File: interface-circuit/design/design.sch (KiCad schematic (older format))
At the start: 30 parts, among them J1 Raspberry_Pi_2_3, J10 Conn_01x02_Male, J11 Conn_01x03_Male, J12 Conn_01x03_Male, J13 Screw_Terminal_01x02, J14 Conn_01x02_Male, J2 Screw_Terminal_01x05, J3 Screw_Terminal_01x05, J4 Conn_02x15_Counter_Clockwise, J5 Conn_02x06_Counter_Clockwise, J6 Conn_01x02_Male, J7 Screw_Terminal_01x02, J8 Screw_Terminal_01x02, J9 Conn_01x02_Male, Q1 2N3904-AP, Q2 2N3904-AP, Q3 2N3904-AP, SW1 SW_SPST, SW2 SW_SPST, U1 LogicLevelConverter_BOB-08745

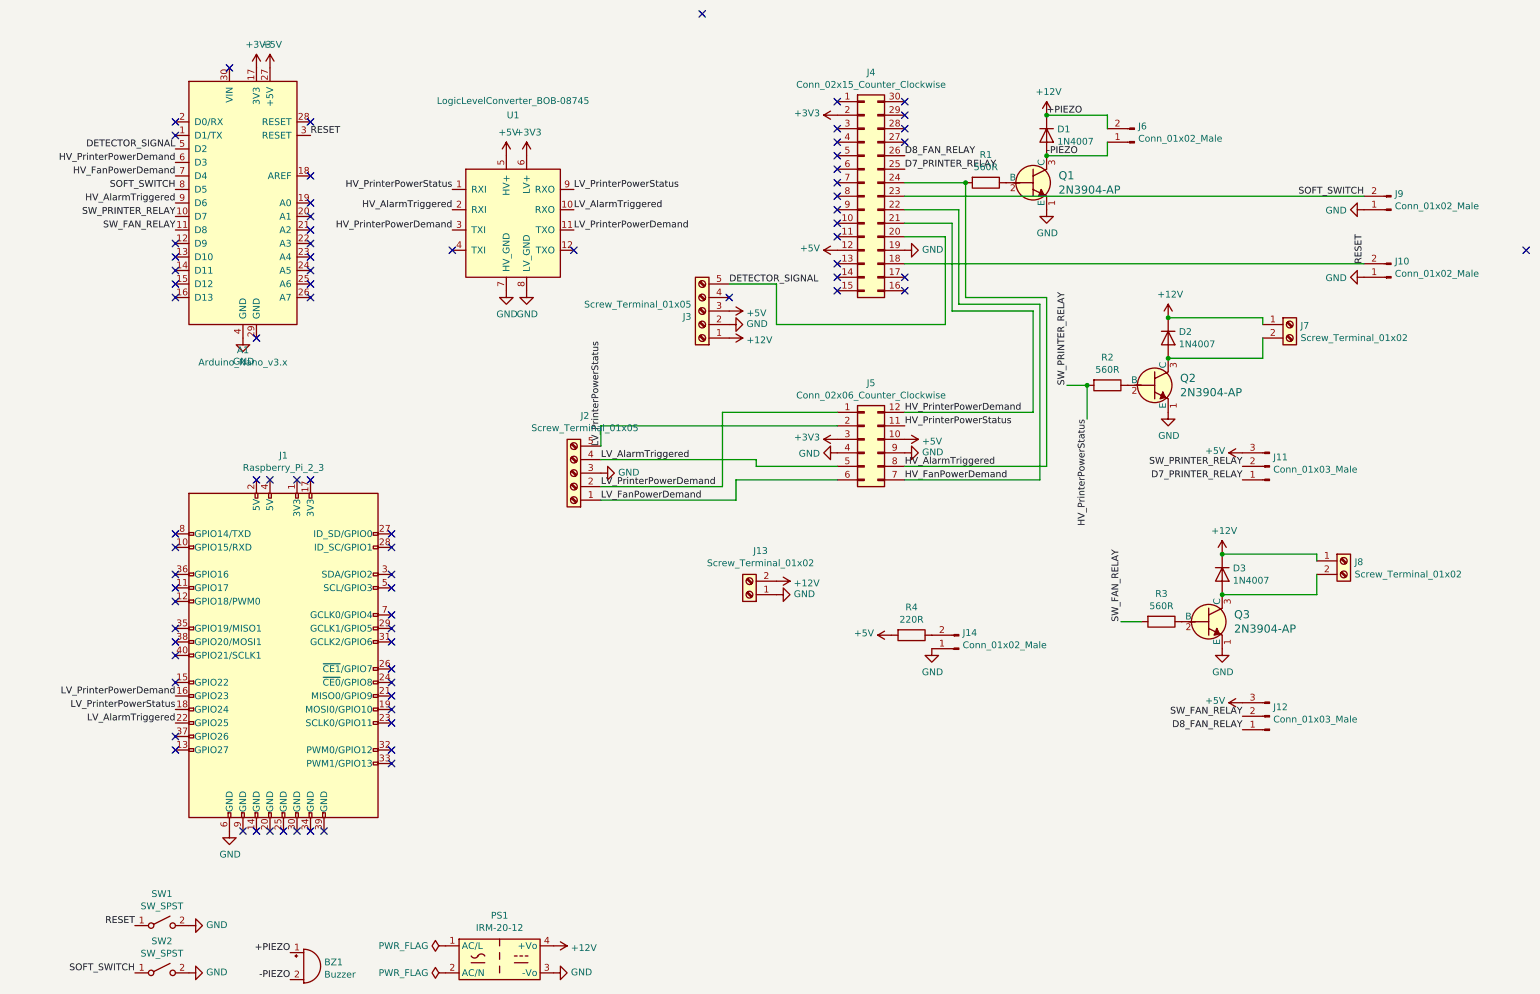
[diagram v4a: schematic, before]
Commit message: Removed connectors between Arduino and shifter, header strips will be soldered in under them
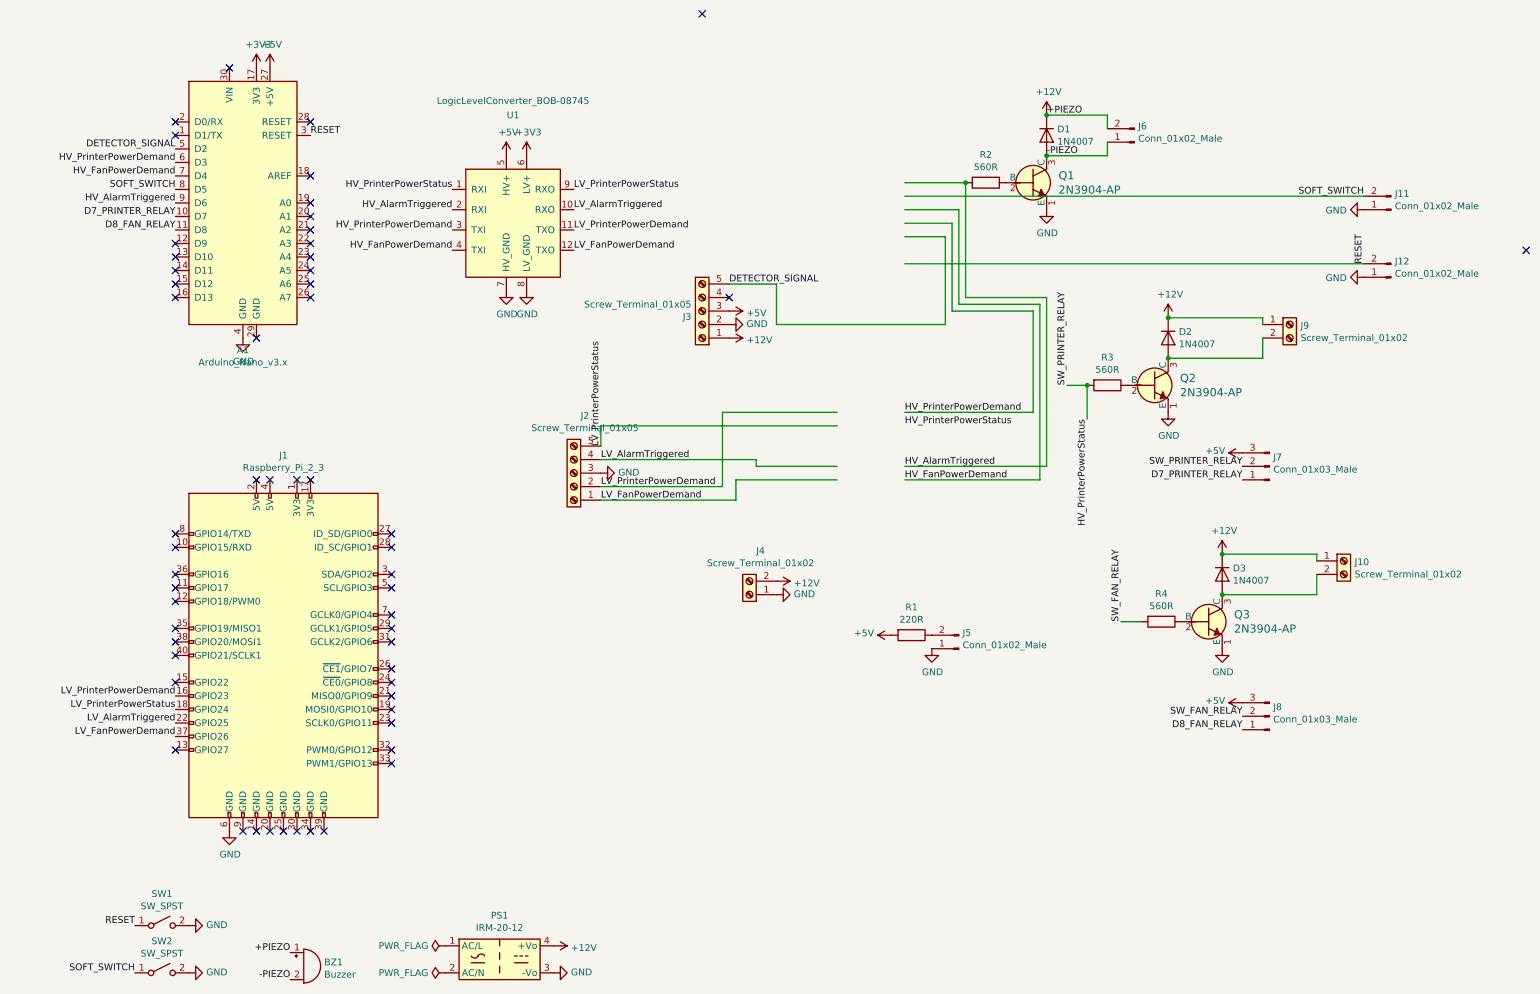
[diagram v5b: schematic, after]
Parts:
- removed J4: Conn_02x15_Counter_Clockwise, symbol Connector_Generic:Conn_02x15_Counter_Clockwise
- removed J5: Conn_02x06_Counter_Clockwise, symbol Connector_Generic:Conn_02x06_Counter_Clockwise
- renumbered J8 to J10, J9 to J11, J10 to J12, J13 to J4, J14 to J5, J11 to J7, J12 to J8, J7 to J9, R4 to R1, R1 to R2, R2 to R3, R3 to R4
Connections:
- no-connect marks 79 -> 57

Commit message: Cleanup
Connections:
- wire segments 48 -> 16
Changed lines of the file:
@@
 LV_AlarmTriggered
 Wire Wire Line
-	4650 3800 5550 3800
-Wire Wire Line
-	5550 3800 5550 3250
-Wire Wire Line
-	5550 3250 6400 3250
-Wire Wire Line
 	4650 3500 4650 3350
-Wire Wire Line
-	4650 3350 6400 3350
-Wire Wire Line
-	4650 3600 5800 3600
-Wire Wire Line
-	5800 3600 5800 3650
 $Comp
 L power:GND #PWR013
@@
 Text Label 4450 1900 0    50   ~ 0
 LV_PrinterPowerDemand
-Text Label 6900 3250 0    50   ~ 0
-HV_PrinterPowerDemand
-Text Label 6900 3350 0    50   ~ 0
-HV_PrinterPowerStatus
 $Comp
 L Connector:Conn_01x02_Male J12
@@
 NoConn ~ 5400 300
 NoConn ~ 5600 2400
-Wire Wire Line
-	5600 2300 5950 2300
-Wire Wire Line
-	5950 2300 5950 2600
-Wire Wire Line
-	5950 2600 7200 2600
-Wire Wire Line
-	7200 2600 7200 1950
-Wire Wire Line
-	7200 1950 6900 1950
-Wire Wire Line
-	6900 3250 7850 3250
-Wire Wire Line
-	7850 3250 7850 2500
-Wire Wire Line
-	7850 2500 7250 2500
-Wire Wire Line
-	7250 2500 7250 1850
-Wire Wire Line
-	7250 1850 6900 1850
 $Comp
 L Connector:Screw_Terminal_01x05 J2
@@
 	-1   0    0    1
 $EndComp
-Wire Wire Line
-	4650 3900 5650 3900
-Wire Wire Line
-	5650 3900 5650 3750
 Text Label 4650 3900 0    50   ~ 0
 LV_FanPowerDemand
-Wire Wire Line
-	7900 2450 7300 2450
-Wire Wire Line
-	7300 2450 7300 1750
-Wire Wire Line
-	7300 1750 6900 1750
-Wire Wire Line
-	6900 2150 10300 2150
 NoConn ~ 11500 2050
 $Comp
@@
 	0    1    1    0
 $EndComp
-Wire Wire Line
-	6900 1650 10300 1650
 Text Label 10300 1650 2    50   ~ 0
 SOFT_SWITCH
@@
 Text Label 1200 7400 2    50   ~ 0
 SOFT_SWITCH
-Wire Wire Line
-	7950 2400 7350 2400
-Wire Wire Line
-	7350 2400 7350 1550
-Wire Wire Line
-	7350 1550 6900 1550
 $Comp
 L Device:R R2
@@
 	0    1    1    0
 $EndComp
-Connection ~ 7350 1550
 $Comp
 L dk_Transistors-Bipolar-BJT-Single:2N3904-AP Q1
@@
 	0    -1   -1   0
 $EndComp
-Wire Wire Line
-	7950 3650 7950 2400
-Wire Wire Line
-	6900 3650 7950 3650
-Wire Wire Line
-	7900 3750 7900 2450
-Wire Wire Line
-	6900 3750 7900 3750
-Text Label 6900 3750 0    50   ~ 0
-HV_FanPowerDemand
-Wire Wire Line
-	5650 3750 6400 3750
-Text Label 6900 3650 0    50   ~ 0
-HV_AlarmTriggered
-Wire Wire Line
-	5800 3650 6400 3650
 Text Label 1500 5650 2    50   ~ 0
 LV_FanPowerDemand
@@
 Text Label 3550 2050 2    50   ~ 0
 HV_FanPowerDemand
+Text Label 7350 1550 2    50   ~ 0
+HV_AlarmTriggered
 $EndSCHEMATC

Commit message: Associated all components that will go on the protoboard
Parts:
- BZ1: footprint (none) -> Buzzer_Beeper:Buzzer_15x7.5RM7.6
- J10, J4, J9: footprint (none) -> Connectors:SCREWTERMINAL-5MM-2
- J11, J12, J5, J6: footprint (none) -> Connector_PinHeader_2.54mm:PinHeader_1x02_P2.54mm_Vertical
- J2, J3: footprint (none) -> Connectors:SCREWTERMINAL-3.5MM-5
- J7, J8: footprint (none) -> Connector_PinHeader_2.54mm:PinHeader_1x03_P2.54mm_Vertical
- R1, R2, R3, R4: footprint (none) -> Resistor_THT:R_Axial_DIN0207_L6.3mm_D2.5mm_P10.16mm_Horizontal
- U1: footprint (none) -> custom-footprints:LOGIC_LEVEL_CONVERTER_BOB11978_BOB8745_XC4486
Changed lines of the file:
@@
 F 0 "U1" H 4000 2650 50  0000 C CNN
 F 1 "LogicLevelConverter_BOB-08745" H 4000 2756 50  0000 C CNN
-F 2 "" H 3350 2600 50  0001 C CNN
+F 2 "custom-footprints:LOGIC_LEVEL_CONVERTER_BOB11978_BOB8745_XC4486" H 3350 2600 50  0001 C CNN
 F 3 "" H 3350 2600 50  0001 C CNN
 	1    4000 1850
@@
 F 0 "J12" H 10472 2132 50  0000 R CNN
 F 1 "Conn_01x02_Male" H 10472 2223 50  0000 R CNN
-F 2 "" H 10500 2250 50  0001 C CNN
+F 2 "Connector_PinHeader_2.54mm:PinHeader_1x02_P2.54mm_Vertical" H 10500 2250 50  0001 C CNN
 F 3 "~" H 10500 2250 50  0001 C CNN
 	1    10500 2250
@@
 F 0 "J3" H 5480 2542 50  0000 L CNN
 F 1 "Screw_Terminal_01x05" H 5480 2451 50  0000 L CNN
-F 2 "" H 5400 2500 50  0001 C CNN
+F 2 "Connectors:SCREWTERMINAL-3.5MM-5" H 5400 2500 50  0001 C CNN
 F 3 "~" H 5400 2500 50  0001 C CNN
 	1    5400 2500
@@
 F 0 "J2" H 4368 3275 50  0000 C CNN
 F 1 "Screw_Terminal_01x05" H 4368 3366 50  0000 C CNN
-F 2 "" H 4450 3700 50  0001 C CNN
+F 2 "Connectors:SCREWTERMINAL-3.5MM-5" H 4450 3700 50  0001 C CNN
 F 3 "~" H 4450 3700 50  0001 C CNN
 	1    4450 3700
@@
 F 0 "J11" H 10472 1632 50  0000 R CNN
 F 1 "Conn_01x02_Male" H 10472 1723 50  0000 R CNN
-F 2 "" H 10500 1750 50  0001 C CNN
+F 2 "Connector_PinHeader_2.54mm:PinHeader_1x02_P2.54mm_Vertical" H 10500 1750 50  0001 C CNN
 F 3 "~" H 10500 1750 50  0001 C CNN
 	1    10500 1750
@@
 F 0 "R2" V 7293 1550 50  0000 C CNN
 F 1 "560R" V 7384 1550 50  0000 C CNN
-F 2 "" V 7430 1550 50  0001 C CNN
+F 2 "Resistor_THT:R_Axial_DIN0207_L6.3mm_D2.5mm_P10.16mm_Horizontal" V 7430 1550 50  0001 C CNN
 F 3 "~" H 7500 1550 50  0001 C CNN
 	1    7500 1550
@@
 F 0 "J6" H 8572 1132 50  0000 R CNN
 F 1 "Conn_01x02_Male" H 8572 1223 50  0000 R CNN
-F 2 "" H 8600 1250 50  0001 C CNN
+F 2 "Connector_PinHeader_2.54mm:PinHeader_1x02_P2.54mm_Vertical" H 8600 1250 50  0001 C CNN
 F 3 "~" H 8600 1250 50  0001 C CNN
 	1    8600 1250
@@
 F 0 "BZ1" H 2602 7379 50  0000 L CNN
 F 1 "Buzzer" H 2602 7288 50  0000 L CNN
-F 2 "" V 2425 7450 50  0001 C CNN
+F 2 "Buzzer_Beeper:Buzzer_15x7.5RM7.6" V 2425 7450 50  0001 C CNN
 F 3 "~" V 2425 7450 50  0001 C CNN
 	1    2450 7350
@@
 F 0 "R3" V 8193 3050 50  0000 C CNN
 F 1 "560R" V 8284 3050 50  0000 C CNN
-F 2 "" V 8330 3050 50  0001 C CNN
+F 2 "Resistor_THT:R_Axial_DIN0207_L6.3mm_D2.5mm_P10.16mm_Horizontal" V 8330 3050 50  0001 C CNN
 F 3 "~" H 8400 3050 50  0001 C CNN
 	1    8400 3050
@@
 F 0 "J9" H 9830 2592 50  0000 L CNN
 F 1 "Screw_Terminal_01x02" H 9830 2501 50  0000 L CNN
-F 2 "" H 9750 2600 50  0001 C CNN
+F 2 "Connectors:SCREWTERMINAL-5MM-2" H 9750 2600 50  0001 C CNN
 F 3 "~" H 9750 2600 50  0001 C CNN
 	1    9750 2600
@@
 F 0 "R4" V 8593 4800 50  0000 C CNN
 F 1 "560R" V 8684 4800 50  0000 C CNN
-F 2 "" V 8730 4800 50  0001 C CNN
+F 2 "Resistor_THT:R_Axial_DIN0207_L6.3mm_D2.5mm_P10.16mm_Horizontal" V 8730 4800 50  0001 C CNN
 F 3 "~" H 8800 4800 50  0001 C CNN
 	1    8800 4800
@@
 F 0 "J10" H 10230 4342 50  0000 L CNN
 F 1 "Screw_Terminal_01x02" H 10230 4251 50  0000 L CNN
-F 2 "" H 10150 4350 50  0001 C CNN
+F 2 "Connectors:SCREWTERMINAL-5MM-2" H 10150 4350 50  0001 C CNN
 F 3 "~" H 10150 4350 50  0001 C CNN
 	1    10150 4350
@@
 F 0 "J7" H 9572 3582 50  0000 R CNN
 F 1 "Conn_01x03_Male" H 9572 3673 50  0000 R CNN
-F 2 "" H 9600 3650 50  0001 C CNN
+F 2 "Connector_PinHeader_2.54mm:PinHeader_1x03_P2.54mm_Vertical" H 9600 3650 50  0001 C CNN
 F 3 "~" H 9600 3650 50  0001 C CNN
 	1    9600 3650
@@
 F 0 "J8" H 9572 5432 50  0000 R CNN
 F 1 "Conn_01x03_Male" H 9572 5523 50  0000 R CNN
-F 2 "" H 9600 5500 50  0001 C CNN
+F 2 "Connector_PinHeader_2.54mm:PinHeader_1x03_P2.54mm_Vertical" H 9600 5500 50  0001 C CNN
 F 3 "~" H 9600 5500 50  0001 C CNN
 	1    9600 5500
@@
 F 0 "J4" H 5668 4275 50  0000 C CNN
 F 1 "Screw_Terminal_01x02" H 5668 4366 50  0000 C CNN
-F 2 "" H 5750 4600 50  0001 C CNN
+F 2 "Connectors:SCREWTERMINAL-5MM-2" H 5750 4600 50  0001 C CNN
 F 3 "~" H 5750 4600 50  0001 C CNN
 	1    5750 4600
@@
 F 0 "R1" V 6743 4900 50  0000 C CNN
 F 1 "220R" V 6834 4900 50  0000 C CNN
-F 2 "" V 6880 4900 50  0001 C CNN
+F 2 "Resistor_THT:R_Axial_DIN0207_L6.3mm_D2.5mm_P10.16mm_Horizontal" V 6880 4900 50  0001 C CNN
 F 3 "~" H 6950 4900 50  0001 C CNN
 	1    6950 4900
@@
 F 0 "J5" H 7272 4882 50  0000 R CNN
 F 1 "Conn_01x02_Male" H 7272 4973 50  0000 R CNN
-F 2 "" H 7300 5000 50  0001 C CNN
+F 2 "Connector_PinHeader_2.54mm:PinHeader_1x02_P2.54mm_Vertical" H 7300 5000 50  0001 C CNN
 F 3 "~" H 7300 5000 50  0001 C CNN
 	1    7300 5000

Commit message: Had to number pins on custom footprint to get netlist to work
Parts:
- BZ1: footprint Buzzer_Beeper:Buzzer_15x7.5RM7.6 -> (none)
- PS1: footprint Converter_ACDC:Converter_ACDC_MeanWell_IRM-20-xx_THT -> (none)
- U1: footprint custom-footprints:LOGIC_LEVEL_CONVERTER_BOB11978_BOB8745_XC4486 -> custom-footprints:LOGIC_LEVEL_CONVERTER_BOB-8745
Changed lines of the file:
@@
 F 0 "U1" H 4000 2650 50  0000 C CNN
 F 1 "LogicLevelConverter_BOB-08745" H 4000 2756 50  0000 C CNN
-F 2 "custom-footprints:LOGIC_LEVEL_CONVERTER_BOB11978_BOB8745_XC4486" H 3350 2600 50  0001 C CNN
+F 2 "custom-footprints:LOGIC_LEVEL_CONVERTER_BOB-8745" H 3350 2600 50  0001 C CNN
 F 3 "" H 3350 2600 50  0001 C CNN
 	1    4000 1850
@@
 Text Label 10300 2150 1    50   ~ 0
 RESET
-Text Label 1200 7050 2    50   ~ 0
-RESET
-$Comp
-L power:GND #PWR01
-U 1 1 5CC93EB0
-P 1600 7050
-F 0 "#PWR01" H 1600 6800 50  0001 C CNN
-F 1 "GND" V 1605 6922 50  0000 R CNN
-F 2 "" H 1600 7050 50  0001 C CNN
-F 3 "" H 1600 7050 50  0001 C CNN
-	1    1600 7050
-	0    -1   -1   0
-$EndComp
-$Comp
-L Switch:SW_SPST SW1
-U 1 1 5CC93548
-P 1400 7050
-F 0 "SW1" H 1400 7285 50  0000 C CNN
-F 1 "SW_SPST" H 1400 7194 50  0000 C CNN
-F 2 "" H 1400 7050 50  0001 C CNN
-F 3 "~" H 1400 7050 50  0001 C CNN
-	1    1400 7050
-	1    0    0    -1
-$EndComp
 $Comp
 L Connector:Screw_Terminal_01x05 J3
@@
 $EndComp
 Text Label 10300 1650 2    50   ~ 0
-SOFT_SWITCH
-$Comp
-L Switch:SW_SPST SW2
-U 1 1 5CCFC122
-P 1400 7400
-F 0 "SW2" H 1400 7635 50  0000 C CNN
-F 1 "SW_SPST" H 1400 7544 50  0000 C CNN
-F 2 "" H 1400 7400 50  0001 C CNN
-F 3 "~" H 1400 7400 50  0001 C CNN
-	1    1400 7400
-	1    0    0    -1
-$EndComp
-$Comp
-L power:GND #PWR02
-U 1 1 5CCFCAEC
-P 1600 7400
-F 0 "#PWR02" H 1600 7150 50  0001 C CNN
-F 1 "GND" V 1605 7272 50  0000 R CNN
-F 2 "" H 1600 7400 50  0001 C CNN
-F 3 "" H 1600 7400 50  0001 C CNN
-	1    1600 7400
-	0    -1   -1   0
-$EndComp
-Text Label 1200 7400 2    50   ~ 0
 SOFT_SWITCH
 $Comp
@@
 +PIEZO
 Text Label 7950 1350 0    50   ~ 0
--PIEZO
-$Comp
-L Device:Buzzer BZ1
-U 1 1 5CC343CA
-P 2450 7350
-F 0 "BZ1" H 2602 7379 50  0000 L CNN
-F 1 "Buzzer" H 2602 7288 50  0000 L CNN
-F 2 "Buzzer_Beeper:Buzzer_15x7.5RM7.6" V 2425 7450 50  0001 C CNN
-F 3 "~" V 2425 7450 50  0001 C CNN
-	1    2450 7350
-	1    0    0    -1
-$EndComp
-Text Label 2350 7250 2    50   ~ 0
-+PIEZO
-Text Label 2350 7450 2    50   ~ 0
 -PIEZO
 $Comp
@@
 SW_FAN_RELAY
 $Comp
-L Converter_ACDC:IRM-20-12 PS1
-U 1 1 5CCE2BB6
-P 3900 7300
-F 0 "PS1" H 3900 7625 50  0000 C CNN
-F 1 "IRM-20-12" H 3900 7534 50  0000 C CNN
-F 2 "Converter_ACDC:Converter_ACDC_MeanWell_IRM-20-xx_THT" H 3900 7000 50  0001 C CNN
-F 3 "http://www.meanwell.com/Upload/PDF/IRM-20/IRM-20-SPEC.PDF" H 4300 6950 50  0001 C CNN
-	1    3900 7300
-	1    0    0    -1
-$EndComp
-$Comp
-L power:+12V #PWR011
-U 1 1 5CCE3D4A
-P 4300 7200
-F 0 "#PWR011" H 4300 7050 50  0001 C CNN
-F 1 "+12V" V 4315 7328 50  0000 L CNN
-F 2 "" H 4300 7200 50  0001 C CNN
-F 3 "" H 4300 7200 50  0001 C CNN
-	1    4300 7200
-	0    1    1    0
-$EndComp
-$Comp
-L power:GND #PWR012
-U 1 1 5CCE46FE
-P 4300 7400
-F 0 "#PWR012" H 4300 7150 50  0001 C CNN
-F 1 "GND" V 4305 7272 50  0000 R CNN
-F 2 "" H 4300 7400 50  0001 C CNN
-F 3 "" H 4300 7400 50  0001 C CNN
-	1    4300 7400
-	0    -1   -1   0
-$EndComp
-$Comp
 L Connector:Screw_Terminal_01x02 J4
 U 1 1 5CCF3969
@@
 Text Label 5600 2300 0    50   ~ 0
 DETECTOR_SIGNAL
+Text Label 1500 5650 2    50   ~ 0
+LV_FanPowerDemand
+Text Label 4450 2050 0    50   ~ 0
+LV_FanPowerDemand
+Text Label 3550 2050 2    50   ~ 0
+HV_FanPowerDemand
+Text Label 7350 1550 2    50   ~ 0
+HV_AlarmTriggered
+$Comp
+L power:PWR_FLAG #FLG02
+U 1 1 5CC7DA6D
+P 3500 7400
+F 0 "#FLG02" H 3500 7475 50  0001 C CNN
+F 1 "PWR_FLAG" V 3500 7527 50  0000 L CNN
+F 2 "" H 3500 7400 50  0001 C CNN
+F 3 "~" H 3500 7400 50  0001 C CNN
+	1    3500 7400
+	0    -1   -1   0
+$EndComp
 $Comp
 L power:PWR_FLAG #FLG01
@@
 $EndComp
 $Comp
-L power:PWR_FLAG #FLG02
-U 1 1 5CC7DA6D
-P 3500 7400
-F 0 "#FLG02" H 3500 7475 50  0001 C CNN
-F 1 "PWR_FLAG" V 3500 7527 50  0000 L CNN
-F 2 "" H 3500 7400 50  0001 C CNN
-F 3 "~" H 3500 7400 50  0001 C CNN
-	1    3500 7400
-	0    -1   -1   0
-$EndComp
-Text Label 1500 5650 2    50   ~ 0
-LV_FanPowerDemand
-Text Label 4450 2050 0    50   ~ 0
-LV_FanPowerDemand
-Text Label 3550 2050 2    50   ~ 0
-HV_FanPowerDemand
-Text Label 7350 1550 2    50   ~ 0
-HV_AlarmTriggered
+L power:GND #PWR012
+U 1 1 5CCE46FE
+P 4300 7400
+F 0 "#PWR012" H 4300 7150 50  0001 C CNN
+F 1 "GND" V 4305 7272 50  0000 R CNN
+F 2 "" H 4300 7400 50  0001 C CNN
+F 3 "" H 4300 7400 50  0001 C CNN
+	1    4300 7400
+	0    -1   -1   0
+$EndComp
+$Comp
+L power:+12V #PWR011
+U 1 1 5CCE3D4A
+P 4300 7200
+F 0 "#PWR011" H 4300 7050 50  0001 C CNN
+F 1 "+12V" V 4315 7328 50  0000 L CNN
+F 2 "" H 4300 7200 50  0001 C CNN
+F 3 "" H 4300 7200 50  0001 C CNN
+	1    4300 7200
+	0    1    1    0
+$EndComp
+$Comp
+L Converter_ACDC:IRM-20-12 PS1
+U 1 1 5CCE2BB6
+P 3900 7300
+F 0 "PS1" H 3900 7625 50  0000 C CNN
+F 1 "IRM-20-12" H 3900 7534 50  0000 C CNN
+F 2 "" H 3900 7000 50  0001 C CNN
+F 3 "http://www.meanwell.com/Upload/PDF/IRM-20/IRM-20-SPEC.PDF" H 4300 6950 50  0001 C CNN
+	1    3900 7300
+	1    0    0    -1
+$EndComp
+Text Label 2350 7450 2    50   ~ 0
+-PIEZO
+Text Label 2350 7250 2    50   ~ 0
++PIEZO
+$Comp
+L Device:Buzzer BZ1
+U 1 1 5CC343CA
+P 2450 7350
+F 0 "BZ1" H 2602 7379 50  0000 L CNN
+F 1 "Buzzer" H 2602 7288 50  0000 L CNN
+F 2 "" V 2425 7450 50  0001 C CNN
+F 3 "~" V 2425 7450 50  0001 C CNN
+	1    2450 7350
+	1    0    0    -1
+$EndComp
+Text Label 1200 7400 2    50   ~ 0
+SOFT_SWITCH
+$Comp
+L power:GND #PWR02
+U 1 1 5CCFCAEC
+P 1600 7400
+F 0 "#PWR02" H 1600 7150 50  0001 C CNN
+F 1 "GND" V 1605 7272 50  0000 R CNN
+F 2 "" H 1600 7400 50  0001 C CNN
+F 3 "" H 1600 7400 50  0001 C CNN
+	1    1600 7400
+	0    -1   -1   0
+$EndComp
+$Comp
+L Switch:SW_SPST SW2
+U 1 1 5CCFC122
+P 1400 7400
+F 0 "SW2" H 1400 7635 50  0000 C CNN
+F 1 "SW_SPST" H 1400 7544 50  0000 C CNN
+F 2 "" H 1400 7400 50  0001 C CNN
+F 3 "~" H 1400 7400 50  0001 C CNN
+	1    1400 7400
+	1    0    0    -1
+$EndComp
+$Comp
+L Switch:SW_SPST SW1
+U 1 1 5CC93548
+P 1400 7050
+F 0 "SW1" H 1400 7285 50  0000 C CNN
+F 1 "SW_SPST" H 1400 7194 50  0000 C CNN
+F 2 "" H 1400 7050 50  0001 C CNN
+F 3 "~" H 1400 7050 50  0001 C CNN
+	1    1400 7050
+	1    0    0    -1
+$EndComp
+$Comp
+L power:GND #PWR01
+U 1 1 5CC93EB0
+P 1600 7050
+F 0 "#PWR01" H 1600 6800 50  0001 C CNN
+F 1 "GND" V 1605 6922 50  0000 R CNN
+F 2 "" H 1600 7050 50  0001 C CNN
+F 3 "" H 1600 7050 50  0001 C CNN
+	1    1600 7050
+	0    -1   -1   0
+$EndComp
+Text Label 1200 7050 2    50   ~ 0
+RESET
 $EndSCHEMATC
